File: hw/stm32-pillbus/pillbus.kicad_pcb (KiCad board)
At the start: 2 copper layers, 100 x 100 mm, 40 parts, among them J1 LEDs DI, J2 LEDs DI, J3 LEDs DI, J4 LEDs DI, J5 LEDs DO, J6 LEDs DO, J7 LEDs DO, J8 LEDs DO

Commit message: stm32pill schema
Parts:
- added ADC0: ADC0, base:PTH, F.Cu at (134.6, 76.2)
- added ADC1: ADC0, base:PTH, F.Cu at (83.8, 76.2)
- added ADC2: ADC0, base:PTH, F.Cu at (78.7, 127.0)
- added ADC3: ADC0, base:PTH, F.Cu at (58.4, 76.2)
- added ADC4: ADC0, base:PTH, F.Cu at (109.2, 76.2)
- added AL1: Arduino Left Pins, Connector_PinHeader_2.54mm:PinHeader_1x15_P2.54mm_Vertical, F.Cu at (116.8, 50.8)
- added AL2: Arduino Left Pins, Connector_PinHeader_2.54mm:PinHeader_1x15_P2.54mm_Vertical, F.Cu at (66.0, 50.8)
- added AL3: Arduino Left Pins, Connector_PinHeader_2.54mm:PinHeader_1x15_P2.54mm_Vertical, F.Cu at (61.0, 101.6)
- added AL4: Arduino Left Pins, Connector_PinHeader_2.54mm:PinHeader_1x15_P2.54mm_Vertical, F.Cu at (40.6, 50.8)
- added AL5: Arduino Left Pins, Connector_PinHeader_2.54mm:PinHeader_1x15_P2.54mm_Vertical, F.Cu at (91.4, 50.8)
- added AR1: Arduino Right Pins, Connector_PinHeader_2.54mm:PinHeader_1x15_P2.54mm_Vertical, F.Cu at (137.2, 50.8)
- added AR2: Arduino Right Pins, Connector_PinHeader_2.54mm:PinHeader_1x15_P2.54mm_Vertical, F.Cu at (86.4, 50.8)
- added AR3: Arduino Right Pins, Connector_PinHeader_2.54mm:PinHeader_1x15_P2.54mm_Vertical, F.Cu at (81.3, 101.6)
- added AR4: Arduino Right Pins, Connector_PinHeader_2.54mm:PinHeader_1x15_P2.54mm_Vertical, F.Cu at (61.0, 50.8)
- added AR5: Arduino Right Pins, Connector_PinHeader_2.54mm:PinHeader_1x15_P2.54mm_Vertical, F.Cu at (111.8, 50.8)
- added Boot0: Boot0, base:PTH, F.Cu at (119.4, 66.0)
- added Boot1: Boot0, base:PTH, F.Cu at (68.6, 66.0)
- added Boot2: Boot0, base:PTH, F.Cu at (63.5, 116.8)
- added Boot3: Boot0, base:PTH, F.Cu at (43.2, 66.0)
- added Boot4: Boot0, base:PTH, F.Cu at (94.0, 66.0)
- added I2C_1: I2C_2, Connector_PinHeader_2.54mm:PinHeader_1x02_P2.54mm_Vertical, F.Cu at (83.8, 68.6)
- added I2C_2: I2C_2, Connector_PinHeader_2.54mm:PinHeader_1x02_P2.54mm_Vertical, F.Cu at (134.6, 68.6)
- added I2C_3: I2C_2, Connector_PinHeader_2.54mm:PinHeader_1x02_P2.54mm_Vertical, F.Cu at (78.7, 119.4)
- added I2C_4: I2C_2, Connector_PinHeader_2.54mm:PinHeader_1x02_P2.54mm_Vertical, F.Cu at (58.4, 68.6)
- added I2C_5: I2C_2, Connector_PinHeader_2.54mm:PinHeader_1x02_P2.54mm_Vertical, F.Cu at (109.2, 68.6)
- added NRST1: NRST, base:PTH, F.Cu at (134.6, 78.7)
- added NRST2: NRST, base:PTH, F.Cu at (83.8, 78.7)
- added NRST3: NRST, base:PTH, F.Cu at (78.7, 129.5)
- added NRST4: NRST, base:PTH, F.Cu at (58.4, 78.7)
- added NRST5: NRST, base:PTH, F.Cu at (109.2, 78.7)
- added PC1: PC, Connector_PinHeader_2.54mm:PinHeader_1x03_P2.54mm_Vertical, F.Cu at (129.5, 86.4)
- added PC2: PC, Connector_PinHeader_2.54mm:PinHeader_1x03_P2.54mm_Vertical, F.Cu at (78.7, 86.4)
- added PC3: PC, Connector_PinHeader_2.54mm:PinHeader_1x03_P2.54mm_Vertical, F.Cu at (73.7, 137.2)
- added PC4: PC, Connector_PinHeader_2.54mm:PinHeader_1x03_P2.54mm_Vertical, F.Cu at (53.3, 86.4)
- added PC5: PC, Connector_PinHeader_2.54mm:PinHeader_1x03_P2.54mm_Vertical, F.Cu at (104.1, 86.4)
- added PD1: PD, Connector_PinHeader_2.54mm:PinHeader_1x02_P2.54mm_Vertical, F.Cu at (132.1, 86.4)
- added PD2: PD, Connector_PinHeader_2.54mm:PinHeader_1x02_P2.54mm_Vertical, F.Cu at (81.3, 86.4)
- added PD3: PD, Connector_PinHeader_2.54mm:PinHeader_1x02_P2.54mm_Vertical, F.Cu at (76.2, 137.2)
- added PD4: PD, Connector_PinHeader_2.54mm:PinHeader_1x02_P2.54mm_Vertical, F.Cu at (55.9, 86.4)
- added PD5: PD, Connector_PinHeader_2.54mm:PinHeader_1x02_P2.54mm_Vertical, F.Cu at (106.7, 86.4)
- added SWD1: SWD, Connector_PinHeader_2.54mm:PinHeader_1x02_P2.54mm_Vertical, F.Cu at (121.9, 86.4)
- added SWD2: SWD, Connector_PinHeader_2.54mm:PinHeader_1x02_P2.54mm_Vertical, F.Cu at (71.1, 86.4)
- added SWD3: SWD, Connector_PinHeader_2.54mm:PinHeader_1x02_P2.54mm_Vertical, F.Cu at (66.0, 137.2)
- added SWD4: SWD, Connector_PinHeader_2.54mm:PinHeader_1x02_P2.54mm_Vertical, F.Cu at (45.7, 86.4)
- added SWD5: SWD, Connector_PinHeader_2.54mm:PinHeader_1x02_P2.54mm_Vertical, F.Cu at (96.5, 86.4)
- added U1: STM32F103C8T6, jlcpcb:LQFP-48_L7.0-W7.0-P0.50-LS9.0-BL, F.Cu at (127.0, 72.4)
- added U2: STM32F103C8T6, jlcpcb:LQFP-48_L7.0-W7.0-P0.50-LS9.0-BL, F.Cu at (76.2, 72.4)
- added U3: STM32F103C8T6, jlcpcb:LQFP-48_L7.0-W7.0-P0.50-LS9.0-BL, F.Cu at (71.1, 123.2)
- added U4: STM32F103C8T6, jlcpcb:LQFP-48_L7.0-W7.0-P0.50-LS9.0-BL, F.Cu at (50.8, 72.4)
- added U5: STM32F103C8T6, jlcpcb:LQFP-48_L7.0-W7.0-P0.50-LS9.0-BL, F.Cu at (101.6, 72.4)
- added USB1: USB, Connector_PinHeader_2.54mm:PinHeader_1x02_P2.54mm_Vertical, F.Cu at (119.4, 61.0)
- added USB2: USB, Connector_PinHeader_2.54mm:PinHeader_1x02_P2.54mm_Vertical, F.Cu at (68.6, 61.0)
- added USB3: USB, Connector_PinHeader_2.54mm:PinHeader_1x02_P2.54mm_Vertical, F.Cu at (63.5, 111.8)
- added USB4: USB, Connector_PinHeader_2.54mm:PinHeader_1x02_P2.54mm_Vertical, F.Cu at (43.2, 61.0)
- added USB5: USB, Connector_PinHeader_2.54mm:PinHeader_1x02_P2.54mm_Vertical, F.Cu at (94.0, 61.0)
- added VBAT1: VBAT, base:PTH, F.Cu at (127.0, 86.4)
- added VBAT2: VBAT, base:PTH, F.Cu at (76.2, 86.4)
- added VBAT3: VBAT, base:PTH, F.Cu at (71.1, 137.2)
- added VBAT4: VBAT, base:PTH, F.Cu at (50.8, 86.4)
- added VBAT5: VBAT, base:PTH, F.Cu at (101.6, 86.4)

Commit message: ide stm
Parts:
- removed ADC0, ADC1, ADC2, ADC3, ADC4: ADC0, base:PTH
- removed AL1, AL2, AL3, AL4, AL5: Arduino Left Pins, Connector_PinHeader_2.54mm:PinHeader_1x15_P2.54mm_Vertical
- removed AR1, AR2, AR3, AR4, AR5: Arduino Right Pins, Connector_PinHeader_2.54mm:PinHeader_1x15_P2.54mm_Vertical
- removed Boot0, Boot1, Boot2, Boot3, Boot4: Boot0, base:PTH
- removed I2C_1, I2C_2, I2C_3, I2C_4, I2C_5: I2C_2, Connector_PinHeader_2.54mm:PinHeader_1x02_P2.54mm_Vertical
- removed J1, J2, J3, J4: LEDs DI, base:PTH
- removed J5, J6, J7, J8: LEDs DO, base:PTH
- removed NRST1, NRST2, NRST3, NRST4, NRST5: NRST, base:PTH
- removed PC1, PC2, PC3, PC4, PC5: PC, Connector_PinHeader_2.54mm:PinHeader_1x03_P2.54mm_Vertical
- removed PD1, PD2, PD3, PD4, PD5: PD, Connector_PinHeader_2.54mm:PinHeader_1x02_P2.54mm_Vertical
- removed SWD1, SWD2, SWD3, SWD4, SWD5: SWD, Connector_PinHeader_2.54mm:PinHeader_1x02_P2.54mm_Vertical
- removed USB1, USB2, USB3, USB4, USB5: USB, Connector_PinHeader_2.54mm:PinHeader_1x02_P2.54mm_Vertical
- removed VBAT1, VBAT2, VBAT3, VBAT4, VBAT5: VBAT, base:PTH
- added ?: , , F.Cu at (91.4, 106.7)
- added ?: , , F.Cu at (91.4, 116.8)
- added ?: , , F.Cu at (91.7, 96.5)
- added ?: , , F.Cu at (91.4, 127.0)
- added C1: CL21B103KBANNNC, jlcpcb:C0805, F.Cu at (73.7, 106.4)
- added C10: CL21B103KBANNNC, jlcpcb:C0805, F.Cu at (112.4, 65.1)
- added C11: CL21B103KBANNNC, jlcpcb:C0805, F.Cu at (120.7, 59.7)
- added C12: CL21B103KBANNNC, jlcpcb:C0805, F.Cu at (125.7, 71.1)
- added C13: CL21B103KBANNNC, jlcpcb:C0805, F.Cu at (48.5, 73.7)
- added C14: CL21B103KBANNNC, jlcpcb:C0805, F.Cu at (43.8, 65.1)
- added C15: CL21B103KBANNNC, jlcpcb:C0805, F.Cu at (52.1, 59.7)
- added C16: CL21B103KBANNNC, jlcpcb:C0805, F.Cu at (57.1, 71.1)
- added C17: CL21B103KBANNNC, jlcpcb:C0805, F.Cu at (94.2, 73.7)
- added C18: CL21B103KBANNNC, jlcpcb:C0805, F.Cu at (89.5, 65.1)
- added C19: CL21B103KBANNNC, jlcpcb:C0805, F.Cu at (97.8, 59.7)
- added C2: CL21B103KBANNNC, jlcpcb:C0805, F.Cu at (65.1, 111.1)
- added C20: CL21B103KBANNNC, jlcpcb:C0805, F.Cu at (102.9, 71.1)
- added C3: CL21B103KBANNNC, jlcpcb:C0805, F.Cu at (59.7, 102.9)
- added C4: CL21B103KBANNNC, jlcpcb:C0805, F.Cu at (71.1, 97.8)
- added C5: CL21B103KBANNNC, jlcpcb:C0805, F.Cu at (71.4, 73.7)
- added C6: CL21B103KBANNNC, jlcpcb:C0805, F.Cu at (66.7, 65.1)
- added C7: CL21B103KBANNNC, jlcpcb:C0805, F.Cu at (74.9, 59.7)
- added C8: CL21B103KBANNNC, jlcpcb:C0805, F.Cu at (80.0, 71.1)
- added C9: CL21B103KBANNNC, jlcpcb:C0805, F.Cu at (117.1, 73.7)
- added IDE_STM: IDE, ribbon:IDE STM AB, F.Cu at (40.6, 116.8)
- added J10: IDE STM AB, ribbon:IDE STM AB, F.Cu at (40.6, 94.0)
- added J11: IDE STM CD, ribbon:IDE STM CD, F.Cu at (63.5, 40.6)
- added J12: IDE STM AB, ribbon:IDE STM AB, F.Cu at (83.8, 40.6)
- added J13: IDE STM CD, ribbon:IDE STM CD, F.Cu at (109.2, 40.6)
- added J14: IDE STM AB, ribbon:IDE STM AB, F.Cu at (129.5, 40.6)
- added J15: IDE STM CD, ribbon:IDE STM CD, F.Cu at (40.6, 40.6)
- added J16: IDE STM AB, ribbon:IDE STM AB, F.Cu at (61.0, 40.6)
- added J17: IDE STM CD, ribbon:IDE STM CD, F.Cu at (86.4, 40.6)
- added J18: IDE STM AB, ribbon:IDE STM AB, F.Cu at (106.7, 40.6)
- added J9: IDE STM CD, ribbon:IDE STM CD, F.Cu at (40.6, 114.3)
- added REF**: PTH, base:PTH 1.7mm, F.Cu at (137.4, 126.5)
- added REF**: PTH, base:PTH 1.7mm, F.Cu at (137.4, 136.6)
- added REF**: PTH, base:PTH 1.7mm, F.Cu at (137.4, 106.1)
- added REF**: PTH, base:PTH 1.7mm, F.Cu at (137.4, 116.3)
- moved U3 74.0 mm to (119.1, 66.9)
- moved U1 68.1 mm to (66.9, 104.4), turned to 135 degrees
- moved U5 7.67 mm to (96.3, 66.9)
- moved U2 6.19 mm to (73.4, 66.9)
- moved U4 5.53 mm to (50.5, 66.9)
- moved LED7 0.98 mm to (129.7, 101.5)
- moved LED8 0.98 mm to (135.7, 101.5)
- moved LED1 0.98 mm to (93.7, 101.5)
- moved LED2 0.98 mm to (99.7, 101.5)
- moved LED3 0.98 mm to (105.7, 101.5)
- moved LED4 0.98 mm to (111.7, 101.5)
- moved LED5 0.98 mm to (117.7, 101.5)
- moved LED6 0.98 mm to (123.7, 101.5)
- moved LED15 0.98 mm to (129.6, 111.7)
- moved LED16 0.98 mm to (135.6, 111.7)
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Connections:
- U1 pad 1: (no net) -> /stm32pill/VBAT
- U1 pad 10: (no net) -> Net-(J10-IDE32_STM10)
- U1 pad 11: (no net) -> Net-(J10-IDE30_STM11)
- U1 pad 12: (no net) -> Net-(J10-IDE26_STM12)
- U1 pad 13: (no net) -> Net-(J10-IDE24_STM13)
- U1 pad 14: (no net) -> Net-(J10-IDE22_STM14)
- U1 pad 15: (no net) -> Net-(J10-IDE18_STM15)
- U1 pad 16: (no net) -> Net-(J10-IDE16_STM16)
- U1 pad 17: (no net) -> Net-(J10-IDE14_STM17)
- U1 pad 18: (no net) -> Net-(J10-IDE12_STM18)
- U1 pad 19: (no net) -> Net-(J10-IDE10_STM19)
- U1 pad 2: (no net) -> Net-(J10-IDE40_STM2)
- U1 pad 20: (no net) -> Net-(J10-IDE8_STM20)
- U1 pad 21: /stm32pill/SCL -> Net-(J10-IDE6_STM21)
- U1 pad 22: /stm32pill/SDA -> Net-(J10-IDE4_STM22)
- U1 pad 25: (no net) -> Net-(J9-IDE5_STM25)
- U1 pad 26: (no net) -> Net-(J9-IDE7_STM26)
- U1 pad 27: (no net) -> Net-(J9-IDE9_STM27)
- U1 pad 28: (no net) -> Net-(J9-IDE11_STM28)
- U1 pad 29: (no net) -> Net-(J9-IDE13_STM29)
- U1 pad 3: (no net) -> Net-(J10-IDE38_STM3)
- U1 pad 30: (no net) -> Net-(J9-IDE15_STM30)
- U1 pad 31: (no net) -> Net-(J9-IDE17_STM31)
- U1 pad 32: /stm32pill/USBD- -> Net-(J9-IDE19_STM32)
- U1 pad 33: /stm32pill/USBD+ -> Net-(J9-IDE21_STM33)
- U1 pad 34: (no net) -> Net-(J9-IDE23_STM34)
- U1 pad 37: (no net) -> Net-(J9-IDE25_STM37)
- U1 pad 38: (no net) -> Net-(J9-IDE27_STM38)
- U1 pad 39: (no net) -> Net-(J9-IDE29_STM39)
- U1 pad 4: (no net) -> Net-(J10-IDE36_STM4)
- U1 pad 40: (no net) -> Net-(J9-IDE31_STM40)
- U1 pad 41: (no net) -> Net-(J9-IDE33_STM41)
- U1 pad 42: (no net) -> Net-(J9-IDE35_STM42)
- U1 pad 43: (no net) -> Net-(J9-IDE3_STM43)
- U1 pad 45: (no net) -> Net-(J9-IDE37_STM45)
- U1 pad 46: (no net) -> Net-(J9-IDE39_STM46)
- U1 pad 5: (no net) -> /stm32pill/OSC_IN
- U1 pad 6: (no net) -> /stm32pill/OSC_OUT
- U1 pad 7: (no net) -> /stm32pill/NRST
- U2 pad 1: Net-(U2-VBAT) -> /stm32pill1/VBAT
- U2 pad 21: /stm32pill1/SCL -> Net-(J12-IDE6_STM21)
- U2 pad 22: /stm32pill1/SDA -> Net-(J12-IDE4_STM22)
- U2 pad 32: /stm32pill1/USBD- -> Net-(J11-IDE19_STM32)
- U2 pad 33: /stm32pill1/USBD+ -> Net-(J11-IDE21_STM33)
- U2 pad 5: Net-(PD2-Pin_1) -> /stm32pill1/OSC_IN
- U2 pad 6: Net-(PD2-Pin_2) -> /stm32pill1/OSC_OUT
- U2 pad 7: Net-(NRST2-Pin_1) -> /stm32pill1/NRST
- U3 pad 1: Net-(U3-VBAT) -> /stm32pill2/VBAT
- U3 pad 21: /stm32pill2/SCL -> Net-(J14-IDE6_STM21)
- U3 pad 22: /stm32pill2/SDA -> Net-(J14-IDE4_STM22)
- U3 pad 32: /stm32pill2/USBD- -> Net-(J13-IDE19_STM32)
- U3 pad 33: /stm32pill2/USBD+ -> Net-(J13-IDE21_STM33)
- U3 pad 5: Net-(PD3-Pin_1) -> /stm32pill2/OSC_IN
- U3 pad 6: Net-(PD3-Pin_2) -> /stm32pill2/OSC_OUT
- U3 pad 7: Net-(NRST3-Pin_1) -> /stm32pill2/NRST
- U4 pad 1: Net-(U4-VBAT) -> /stm32pill3/VBAT
- U4 pad 21: /stm32pill3/SCL -> Net-(J16-IDE6_STM21)
- U4 pad 22: /stm32pill3/SDA -> Net-(J16-IDE4_STM22)
- U4 pad 32: /stm32pill3/USBD- -> Net-(J15-IDE19_STM32)
- U4 pad 33: /stm32pill3/USBD+ -> Net-(J15-IDE21_STM33)
- U4 pad 5: Net-(PD4-Pin_1) -> /stm32pill3/OSC_IN
- U4 pad 6: Net-(PD4-Pin_2) -> /stm32pill3/OSC_OUT
- U4 pad 7: Net-(NRST4-Pin_1) -> /stm32pill3/NRST
- U5 pad 1: Net-(U5-VBAT) -> /stm32pill4/VBAT
- U5 pad 21: /stm32pill4/SCL -> Net-(J18-IDE6_STM21)
- U5 pad 22: /stm32pill4/SDA -> Net-(J18-IDE4_STM22)
- U5 pad 32: /stm32pill4/USBD- -> Net-(J17-IDE19_STM32)
- U5 pad 33: /stm32pill4/USBD+ -> Net-(J17-IDE21_STM33)
- U5 pad 5: Net-(PD5-Pin_1) -> /stm32pill4/OSC_IN
- U5 pad 6: Net-(PD5-Pin_2) -> /stm32pill4/OSC_OUT
- U5 pad 7: Net-(NRST5-Pin_1) -> /stm32pill4/NRST
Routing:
- net /leds2/DI: track 2.88 -> 0.00 mm
- net /leds3/DI: track 2.88 -> 0.00 mm
- net /leds0/DI: track 2.88 -> 0.00 mm
- net /leds1/DI: track 2.87 -> 0.00 mm
- net +3.3V: track 256.8 -> 256.1 mm
- net /leds2/DO: track 2.03 -> 1.31 mm
- net /leds1/DO: track 2.07 -> 1.35 mm
- net /leds3/DO: track 2.08 -> 1.38 mm
- net /leds0/DO: track 2.08 -> 1.38 mm

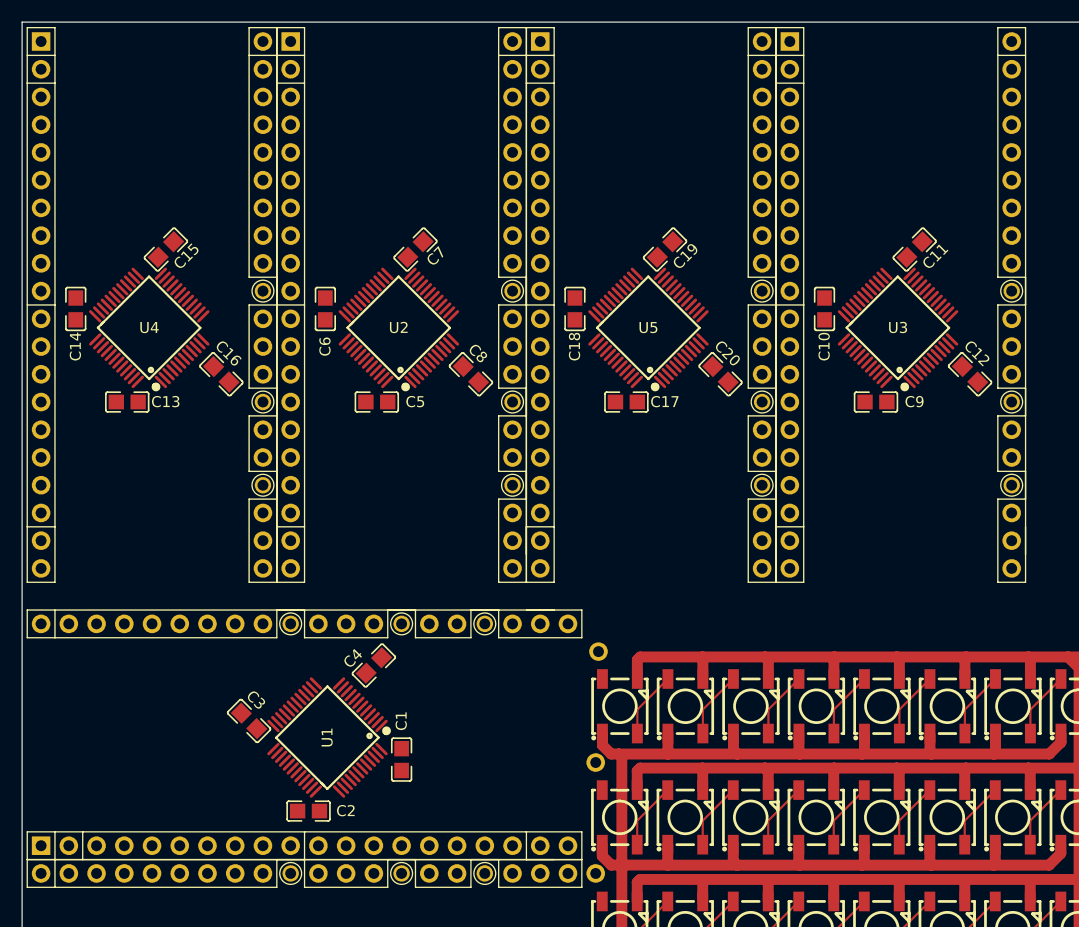
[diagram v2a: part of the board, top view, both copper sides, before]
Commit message: stm32pill pcb
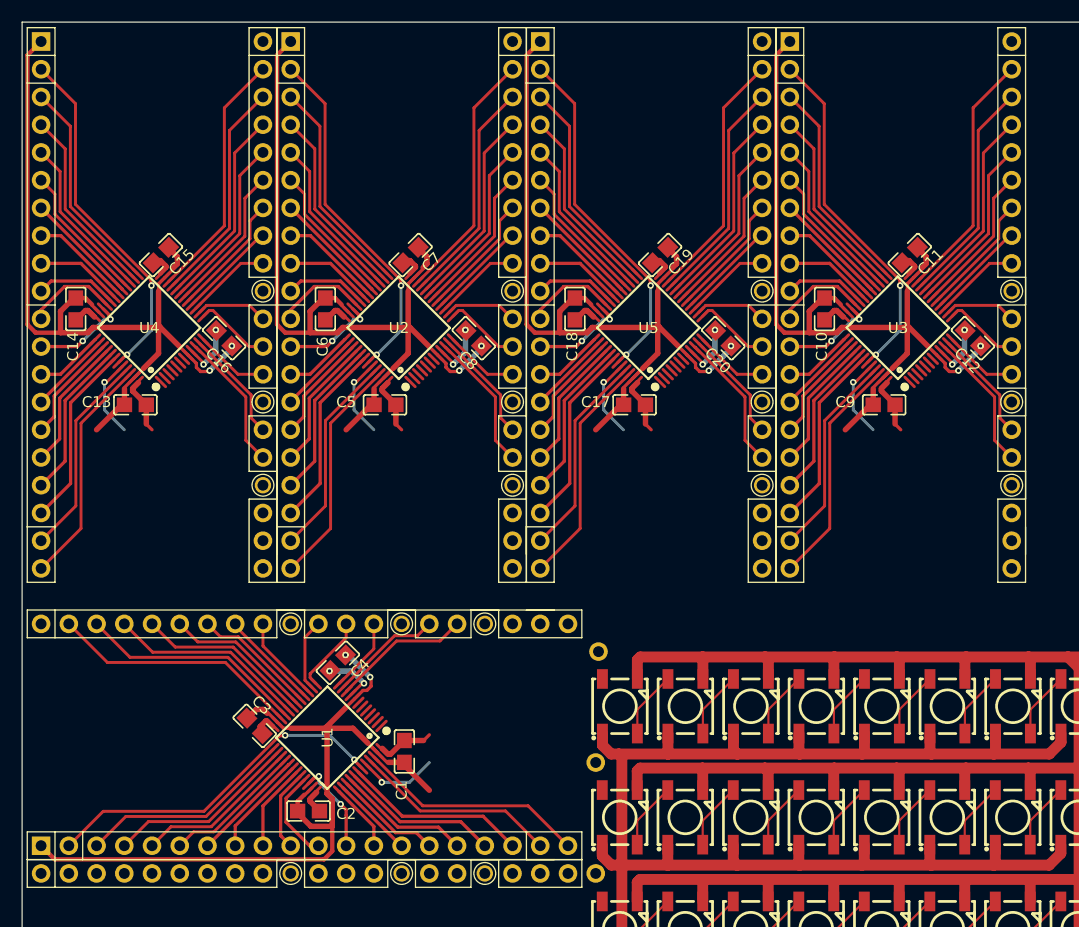
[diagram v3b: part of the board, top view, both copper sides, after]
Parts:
- J10, J12, J14, J16, J18: value IDE STM AB -> IDE
- J11, J13, J15, J17, J9: value IDE STM CD -> IDE
- moved C16 3.31 mm to (57.4, 67.8)
- moved C4 3.31 mm to (67.8, 97.5)
- moved C12 3.31 mm to (126.0, 67.8)
- moved C20 3.31 mm to (103.1, 67.8)
- moved C8 3.31 mm to (80.3, 67.8)
- moved C13 0.79 mm to (49.3, 73.9)
- moved C1 0.79 mm to (73.9, 105.7)
- moved C17 0.79 mm to (95.0, 73.9)
- moved C5 0.79 mm to (72.1, 73.9)
- moved C9 0.79 mm to (117.9, 73.9)
- moved C11 0.68 mm to (120.2, 60.2)
- moved C15 0.68 mm to (51.6, 60.2)
- moved C19 0.68 mm to (97.3, 60.2)
- moved C7 0.68 mm to (74.5, 60.2)
- moved C3 0.68 mm to (60.2, 103.3)
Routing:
- net +3.3V: track 256.1 -> 667.9 mm, vias 0 -> 10
- net GND: track 261.7 -> 344.5 mm, vias 0 -> 10
- net Net-(J9-IDE3_STM43): track 0.00 -> 32.4 mm, vias 0 -> 2
- net Net-(J15-IDE3_STM43): track 0.00 -> 32.4 mm, vias 0 -> 2
- net Net-(J13-IDE3_STM43): track 0.00 -> 32.4 mm, vias 0 -> 2
- net Net-(J17-IDE3_STM43): track 0.00 -> 32.4 mm, vias 0 -> 2
- net Net-(J11-IDE3_STM43): track 0.00 -> 32.4 mm, vias 0 -> 2
- net Net-(J18-IDE4_STM22): track 0.00 -> 23.0 mm
- net Net-(J16-IDE4_STM22): track 0.00 -> 23.0 mm
- net Net-(J14-IDE4_STM22): track 0.00 -> 23.0 mm
- net Net-(J12-IDE4_STM22): track 0.00 -> 23.0 mm
- net Net-(J10-IDE4_STM22): track 0.00 -> 23.0 mm
- net Net-(J17-IDE39_STM46): track 0.00 -> 21.2 mm
- net Net-(J13-IDE39_STM46): track 0.00 -> 21.2 mm
- net Net-(J11-IDE39_STM46): track 0.00 -> 21.2 mm
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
